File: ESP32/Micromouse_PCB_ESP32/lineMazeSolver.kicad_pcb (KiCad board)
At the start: 2 copper layers, 248.8 x 175.7 mm, 112 parts, among them J1 Power_supply, J2 Conn_01x11_Pin, J3 Motor_Left, J4 Motor_Right, SW1 SW_SPST, SW2 SW_Push, SW3 SW_Push, SW4 SW_Push, U1 AMS1117-5.0, U2 DM-OLED096-636, U3 ESP32-DEVKIT-V1

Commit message: Edited Design
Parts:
- removed the C1 at (61.4, 180.8)
- removed the C1 at (195.1, 180.0)
- removed the C1 at (62.0, 89.1)
- removed the C2 at (195.1, 174.6)
- removed the C2 at (62.1, 83.7)
- removed the C2 at (61.4, 175.5)
- removed the C3 at (54.3, 83.3)
- removed the C3 at (53.7, 175.0)
- removed the C3 at (187.4, 174.2)
- removed the C4 at (56.5, 161.1)
- removed the C4 at (57.1, 69.4)
- removed the C4 at (190.2, 160.3)
- removed the C5 at (71.9, 77.2)
- removed the C5 at (205.0, 168.1)
- removed the C5 at (71.3, 168.9)
- removed the C6 at (68.1, 172.2)
- removed the C6 at (68.7, 80.4)
- removed the C6 at (201.8, 171.3)
- removed the C7 at (200.1, 173.7)
- removed the C7 at (67.1, 82.8)
- removed the C7 at (66.4, 174.5)
- removed the D1 at (104.0, 75.3)
- removed the D1 at (237.1, 166.2)
- removed the D1 at (103.4, 167.1)
- removed the H1 at (54.4, 19.8)
- removed the H1 at (53.8, 111.6)
- removed the H1 at (187.5, 110.7)
- removed the H2 at (233.5, 110.7)
- removed the H2 at (100.4, 19.8)
- removed the H2 at (99.8, 111.6)
- removed the J1 at (54.4, 186.6)
- removed the J1 at (188.0, 185.8)
- removed the J1 at (55.0, 94.9)
- removed the J2 at (97.0, 118.7)
- removed the J2 at (230.7, 117.9)
- removed the J2 at (97.6, 27.0)
- removed the J3 at (46.2, 82.2)
- removed the J3 at (45.6, 174.0)
- removed the J3 at (179.3, 173.1)
- removed the J4 at (108.7, 79.8)
- removed the J4 at (241.8, 170.7)
- removed the J4 at (108.1, 171.5)
- removed the MD1 at (80.0, 164.8)
- removed the MD1 at (213.7, 164.0)
- removed the MD1 at (80.6, 73.1)
- removed the R1 at (215.4, 145.3)
- removed the R1 at (82.3, 54.4)
- removed the R1 at (81.7, 146.1)
- removed the R2 at (70.4, 46.3)
- removed the R2 at (203.4, 137.2)
- removed the R2 at (69.7, 138.0)
- removed the R3 at (70.4, 42.2)
- removed the R3 at (203.4, 133.1)
- removed the R3 at (69.7, 134.0)
- removed the R4 at (69.7, 129.9)
- removed the R4 at (203.4, 129.1)
- removed the R4 at (70.4, 38.2)
- removed the REF** at (123.4, 80.8)
- removed the REF** at (256.5, 171.7)
- removed the REF** at (30.7, 172.6)
- removed the REF** at (31.3, 80.8)
- removed the REF** at (122.8, 172.6)
- removed the REF** at (164.4, 171.7)
- removed the SW1 at (200.5, 186.6)
- removed the SW1 at (66.8, 187.4)
- removed the SW1 at (67.4, 95.7)
- removed the SW2 at (211.9, 186.8)
- removed the SW2 at (78.2, 187.6)
- removed the SW2 at (78.8, 95.9)
- removed the SW3 at (89.2, 95.9)
- removed the SW3 at (88.6, 187.6)
- removed the SW3 at (222.3, 186.8)
- removed the SW4 at (98.9, 187.7)
- removed the SW4 at (232.5, 186.8)
- removed the SW4 at (99.5, 95.9)
- removed the U1 at (56.8, 168.1)
- removed the U1 at (190.4, 167.3)
- removed the U1 at (57.4, 76.4)
- removed the U2 at (86.2, 74.0)
- removed the U2 at (219.2, 164.9)
- removed the U2 at (85.5, 165.8)
- removed the U3 at (76.7, 137.7)
- removed the U3 at (210.4, 136.9)
- removed the U3 at (77.3, 46.0)
- moved C3 80.9 mm to (117.1, 121.7)
- moved C4 80.9 mm to (119.9, 107.8)
- moved J1 80.9 mm to (117.7, 133.3)
- moved J3 80.9 mm to (109.0, 120.7)
- moved U1 80.9 mm to (120.1, 114.8)
- moved C2 80.9 mm to (124.8, 122.1)
- moved C5 80.9 mm to (134.7, 115.6)
- moved C6 80.9 mm to (131.5, 118.8)
- moved C7 80.9 mm to (129.8, 121.2)
- moved D1 80.9 mm to (166.8, 113.7)
- moved H1 80.9 mm to (117.2, 58.2)
- moved H2 80.9 mm to (163.2, 58.2)
- moved J2 80.9 mm to (160.4, 65.4)
- moved J4 80.9 mm to (171.5, 118.2)
- moved MD1 80.9 mm to (143.4, 111.5)
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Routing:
- net /3V3: track 529.6 -> 132.4 mm, vias 8 -> 2
- net /SW1: track 457.3 -> 114.3 mm
- net /SW3: track 442.6 -> 110.7 mm
- net /SW2: track 438.7 -> 109.7 mm
- net +5V: track 370.2 -> 92.6 mm, vias 8 -> 2
- net /ML2: track 187.5 -> 46.9 mm, vias 8 -> 2
- net /ML1: track 167.1 -> 41.8 mm, vias 8 -> 2
- net +7.5V: track 146.1 -> 36.5 mm
- net /MR1: track 119.5 -> 29.9 mm, vias 8 -> 2
- net /SDA: track 115.6 -> 28.9 mm
- net Net-(D1-A): track 115.3 -> 28.8 mm
- net /MR2: track 102.7 -> 25.7 mm, vias 8 -> 2
- net /SCL: track 87.5 -> 21.9 mm
- net /LED: track 72.1 -> 18.0 mm
- net /A7: track 27.8 -> 6.94 mm
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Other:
- board size 248.8 x 175.7 mm -> 114 x 84 mm

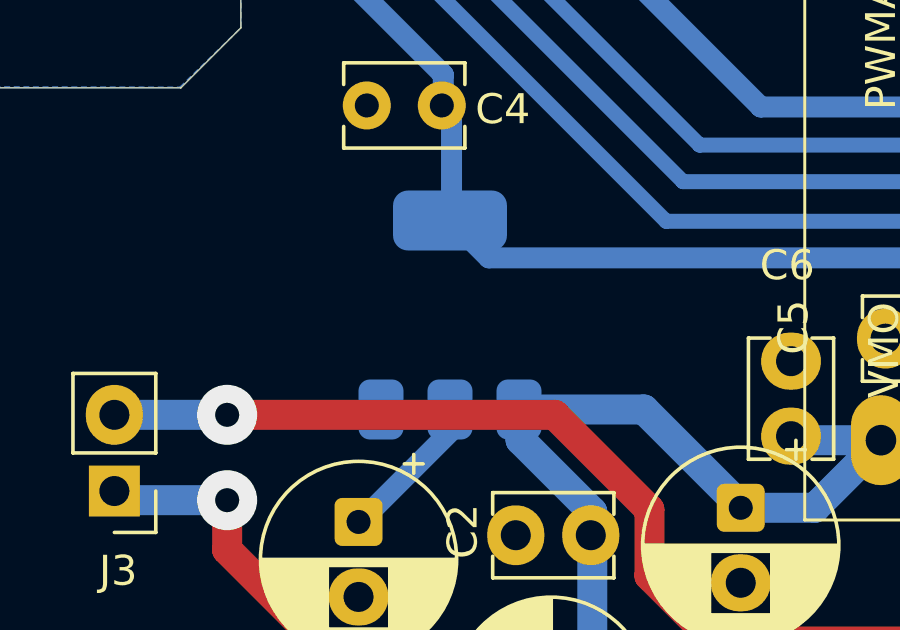
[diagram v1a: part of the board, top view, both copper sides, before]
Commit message: Added PCB Design for Arduino nano
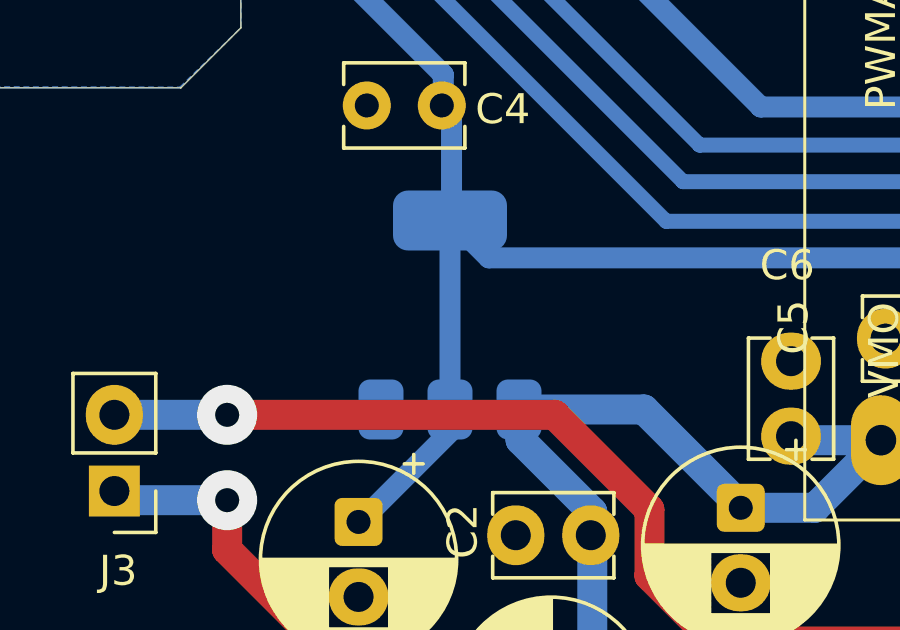
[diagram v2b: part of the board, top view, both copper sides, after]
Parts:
- turned U1 to 180 degrees
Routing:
- net +5V: track 92.6 -> 98.9 mm
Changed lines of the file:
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@@
 			(subtractmaskfromsilk no)
 			(outputformat 4)
-			(mirror no)
+			(mirror yes)
 			(drillshape 2)
 			(scaleselection 1)
@@
 	(footprint "Package_TO_SOT_SMD:SOT-223-3_TabPin2"
 		(layer "B.Cu")
-		(at 120.146666 114.7822 90)
+		(at 120.146666 114.7822 180)
 		(descr "module CMS SOT223 4 pins")
 		(tags "CMS SOT")
 		(property "Reference" "U1"
-			(at 0 4.5 90)
+			(at -4.5 0 90)
 			(layer "B.SilkS")
 			(effects
@@
 		)
 		(property "Value" "AMS1117-5.0"
-			(at 0 -4.5 90)
+			(at 4.5 0 270)
 			(layer "B.Fab")
 			(effects
@@
 		)
 		(property "Datasheet" "http://www.advanced-monolithic.com/pdf/ds1117.pdf"
-			(at 0 0 270)
+			(at 0 0 0)
 			(unlocked yes)
 			(layer "B.Fab")
@@
 		)
 		(property "Description" "1A Low Dropout regulator, positive, 5.0V fixed output, SOT-223"
-			(at 0 0 270)
+			(at 0 0 0)
 			(unlocked yes)
 			(layer "B.Fab")
@@
 		(attr smd)
 		(fp_line
-			(start 1.91 -3.41)
-			(end 1.91 -2.15)
+			(start 3.41 1.91)
+			(end 2.15 1.91)
 			(stroke
 				(width 0.12)
@@
 		)
 		(fp_line
-			(start -1.85 -3.41)
-			(end 1.91 -3.41)
+			(start 3.41 -1.85)
+			(end 3.41 1.91)
 			(stroke
 				(width 0.12)
@@
 		)
 		(fp_line
-			(start 1.91 3.41)
-			(end 1.91 2.15)
+			(start -3.41 1.91)
+			(end -2.15 1.91)
 			(stroke
 				(width 0.12)
@@
 		)
 		(fp_line
-			(start -1.85 3.41)
-			(end 1.91 3.41)
+			(start -3.41 -1.85)
+			(end -3.41 1.91)
 			(stroke
 				(width 0.12)
@@
 		(fp_poly
 			(pts
-				(xy -3.13 3.31) (xy -3.37 3.64) (xy -2.89 3.64) (xy -3.13 3.31)
+				(xy 3.31 -3.13) (xy 3.64 -3.37) (xy 3.64 -2.89) (xy 3.31 -3.13)
 			)
 			(stroke
@@
 		)
 		(fp_line
-			(start 4.4 -3.6)
-			(end 4.4 3.6)
+			(start 3.6 4.4)
+			(end 3.6 -4.4)
 			(stroke
 				(width 0.05)
@@
 		)
 		(fp_line
-			(start -4.4 -3.6)
-			(end 4.4 -3.6)
+			(start 3.6 -4.4)
+			(end -3.6 -4.4)
 			(stroke
 				(width 0.05)
@@
 		)
 		(fp_line
-			(start 4.4 3.6)
-			(end -4.4 3.6)
+			(start -3.6 4.4)
+			(end 3.6 4.4)
 			(stroke
 				(width 0.05)
@@
 		)
 		(fp_line
-			(start -4.4 3.6)
-			(end -4.4 -3.6)
+			(start -3.6 -4.4)
+			(end -3.6 4.4)
 			(stroke
 				(width 0.05)
@@
 		)
 		(fp_line
-			(start -1.85 -3.35)
-			(end 1.85 -3.35)
+			(start 3.35 1.85)
+			(end -3.35 1.85)
 			(stroke
 				(width 0.1)
@@
 		)
 		(fp_line
-			(start -1.85 2.35)
-			(end -1.85 -3.35)
+			(start 3.35 -0.85)
+			(end 3.35 1.85)
 			(stroke
 				(width 0.1)
@@
 		)
 		(fp_line
-			(start -1.85 2.35)
-			(end -0.85 3.35)
+			(start 2.35 -1.85)
+			(end 3.35 -0.85)
 			(stroke
 				(width 0.1)
@@
 		)
 		(fp_line
-			(start 1.85 3.35)
-			(end 1.85 -3.35)
+			(start 2.35 -1.85)
+			(end -3.35 -1.85)
 			(stroke
 				(width 0.1)
@@
 		)
 		(fp_line
-			(start -0.85 3.35)
-			(end 1.85 3.35)
+			(start -3.35 -1.85)
+			(end -3.35 1.85)
 			(stroke
 				(width 0.1)
@@
 		)
 		(fp_text user "${REFERENCE}"
-			(at -1.861 5.505 0)
+			(at -5.505 1.861 0)
 			(layer "B.Fab")
 			(effects
@@
 		)
 		(pad "1" smd roundrect
-			(at -3.15 2.3 90)
+			(at 2.3 -3.15 270)
 			(size 2 1.5)
 			(layers "B.Cu" "B.Mask" "B.Paste")
@@
 		)
 		(pad "2" smd roundrect
-			(at -3.15 0 90)
+			(at 0 -3.15 270)
 			(size 2 1.5)
 			(layers "B.Cu" "B.Mask" "B.Paste")
@@
 		)
 		(pad "2" smd roundrect
-			(at 3.15 0 90)
+			(at 0 3.15 270)
 			(size 2 3.8)
 			(layers "B.Cu" "B.Mask" "B.Paste")
@@
 		)
 		(pad "3" smd roundrect
-			(at -3.15 -2.3 90)
+			(at -2.3 -3.15 270)
 			(size 2 1.5)
 			(layers "B.Cu" "B.Mask" "B.Paste")
@@
 		(width 0.7)
 		(layer "B.Cu")
+		(net 16)
+	)
+	(segment
+		(start 120.146666 117.9322)
+		(end 120.146666 111.6322)
+		(width 0.7)
+		(layer "B.Cu")

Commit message: Added a new features with NANO Based pcb PCB
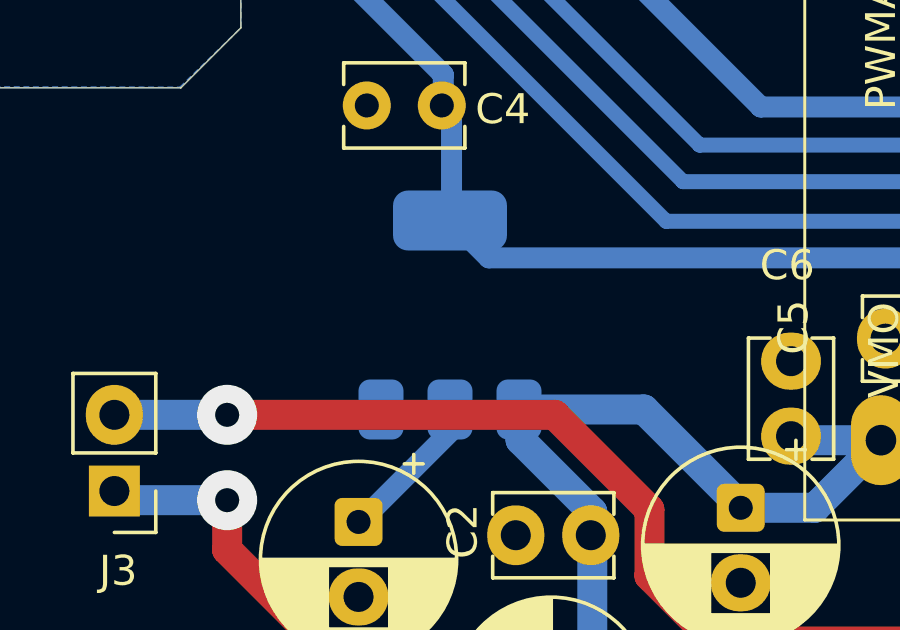
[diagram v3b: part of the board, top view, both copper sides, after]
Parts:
- turned U1 to 90 degrees
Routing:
- net +5V: track 98.9 -> 92.6 mm
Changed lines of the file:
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@@
 			(subtractmaskfromsilk no)
 			(outputformat 4)
-			(mirror yes)
+			(mirror no)
 			(drillshape 2)
 			(scaleselection 1)
@@
 	(footprint "Package_TO_SOT_SMD:SOT-223-3_TabPin2"
 		(layer "B.Cu")
-		(at 120.146666 114.7822 180)
+		(at 120.146666 114.7822 90)
 		(descr "module CMS SOT223 4 pins")
 		(tags "CMS SOT")
 		(property "Reference" "U1"
-			(at -4.5 0 90)
+			(at 0 4.5 90)
 			(layer "B.SilkS")
 			(effects
@@
 		)
 		(property "Value" "AMS1117-5.0"
-			(at 4.5 0 270)
+			(at 0 -4.5 90)
 			(layer "B.Fab")
 			(effects
@@
 		)
 		(property "Datasheet" "http://www.advanced-monolithic.com/pdf/ds1117.pdf"
-			(at 0 0 0)
+			(at 0 0 270)
 			(unlocked yes)
 			(layer "B.Fab")
@@
 		)
 		(property "Description" "1A Low Dropout regulator, positive, 5.0V fixed output, SOT-223"
-			(at 0 0 0)
+			(at 0 0 270)
 			(unlocked yes)
 			(layer "B.Fab")
@@
 		(attr smd)
 		(fp_line
-			(start 3.41 1.91)
-			(end 2.15 1.91)
+			(start 1.91 -3.41)
+			(end 1.91 -2.15)
 			(stroke
 				(width 0.12)
@@
 		)
 		(fp_line
-			(start 3.41 -1.85)
-			(end 3.41 1.91)
+			(start -1.85 -3.41)
+			(end 1.91 -3.41)
 			(stroke
 				(width 0.12)
@@
 		)
 		(fp_line
-			(start -3.41 1.91)
-			(end -2.15 1.91)
+			(start 1.91 3.41)
+			(end 1.91 2.15)
 			(stroke
 				(width 0.12)
@@
 		)
 		(fp_line
-			(start -3.41 -1.85)
-			(end -3.41 1.91)
+			(start -1.85 3.41)
+			(end 1.91 3.41)
 			(stroke
 				(width 0.12)
@@
 		(fp_poly
 			(pts
-				(xy 3.31 -3.13) (xy 3.64 -3.37) (xy 3.64 -2.89) (xy 3.31 -3.13)
+				(xy -3.13 3.31) (xy -3.37 3.64) (xy -2.89 3.64) (xy -3.13 3.31)
 			)
 			(stroke
@@
 		)
 		(fp_line
-			(start 3.6 4.4)
-			(end 3.6 -4.4)
+			(start 4.4 -3.6)
+			(end 4.4 3.6)
 			(stroke
 				(width 0.05)
@@
 		)
 		(fp_line
-			(start 3.6 -4.4)
-			(end -3.6 -4.4)
+			(start -4.4 -3.6)
+			(end 4.4 -3.6)
 			(stroke
 				(width 0.05)
@@
 		)
 		(fp_line
-			(start -3.6 4.4)
-			(end 3.6 4.4)
+			(start 4.4 3.6)
+			(end -4.4 3.6)
 			(stroke
 				(width 0.05)
@@
 		)
 		(fp_line
-			(start -3.6 -4.4)
-			(end -3.6 4.4)
+			(start -4.4 3.6)
+			(end -4.4 -3.6)
 			(stroke
 				(width 0.05)
@@
 		)
 		(fp_line
-			(start 3.35 1.85)
-			(end -3.35 1.85)
+			(start -1.85 -3.35)
+			(end 1.85 -3.35)
 			(stroke
 				(width 0.1)
@@
 		)
 		(fp_line
-			(start 3.35 -0.85)
-			(end 3.35 1.85)
+			(start -1.85 2.35)
+			(end -1.85 -3.35)
 			(stroke
 				(width 0.1)
@@
 		)
 		(fp_line
-			(start 2.35 -1.85)
-			(end 3.35 -0.85)
+			(start -1.85 2.35)
+			(end -0.85 3.35)
 			(stroke
 				(width 0.1)
@@
 		)
 		(fp_line
-			(start 2.35 -1.85)
-			(end -3.35 -1.85)
+			(start 1.85 3.35)
+			(end 1.85 -3.35)
 			(stroke
 				(width 0.1)
@@
 		)
 		(fp_line
-			(start -3.35 -1.85)
-			(end -3.35 1.85)
+			(start -0.85 3.35)
+			(end 1.85 3.35)
 			(stroke
 				(width 0.1)
@@
 		)
 		(fp_text user "${REFERENCE}"
-			(at -5.505 1.861 0)
+			(at -1.861 5.505 0)
 			(layer "B.Fab")
 			(effects
@@
 		)
 		(pad "1" smd roundrect
-			(at 2.3 -3.15 270)
+			(at -3.15 2.3 90)
 			(size 2 1.5)
 			(layers "B.Cu" "B.Mask" "B.Paste")
@@
 		)
 		(pad "2" smd roundrect
-			(at 0 -3.15 270)
+			(at -3.15 0 90)
 			(size 2 1.5)
 			(layers "B.Cu" "B.Mask" "B.Paste")
@@
 		)
 		(pad "2" smd roundrect
-			(at 0 3.15 270)
+			(at 3.15 0 90)
 			(size 2 3.8)
 			(layers "B.Cu" "B.Mask" "B.Paste")
@@
 		)
 		(pad "3" smd roundrect
-			(at -2.3 -3.15 270)
+			(at -3.15 -2.3 90)
 			(size 2 1.5)
 			(layers "B.Cu" "B.Mask" "B.Paste")
@@
 		(width 0.7)
 		(layer "B.Cu")
-		(net 16)
-	)
-	(segment
-		(start 120.146666 117.9322)
-		(end 120.146666 111.6322)
-		(width 0.7)
-		(layer "B.Cu")
